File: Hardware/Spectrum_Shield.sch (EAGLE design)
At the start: 27 parts, among them IC1 MSGEQ7SOIC, IC2 MSGEQ7SOIC, U1 ARDUINO_R3_SHIELD

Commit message: Fixed Ground Issue
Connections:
- net GND: now also AUDIOJACK1.SLEEVE
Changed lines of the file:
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@@
 <?xml version="1.0" encoding="utf-8"?>
 <!DOCTYPE eagle SYSTEM "eagle.dtd">
-<eagle version="7.2.0">
+<eagle version="7.1.0">
 <drawing>
 <settings>
@@
 <layer number="254" name="cooling" color="7" fill="1" visible="yes" active="yes"/>
 </layers>
-<schematic xreflabel="%F%N/%S" xrefpart="/%S">
+<schematic xreflabel="%F%N/%S" xrefpart="/%S.%C%R">
 <attributes>
 </attributes>
@@
 </segment>
 <segment>
+<label x="175.26" y="73.66" size="1.27" layer="95" rot="R180" xref="yes"/>
+<pinref part="AUDIOJACK1" gate="G$1" pin="SLEEVE"/>
 <wire x1="180.34" y1="73.66" x2="175.26" y2="73.66" width="0.1524" layer="91"/>
-<label x="175.26" y="73.66" size="1.27" layer="95" rot="R180" xref="yes"/>
-</segment>
-<segment>
+</segment>
+<segment>

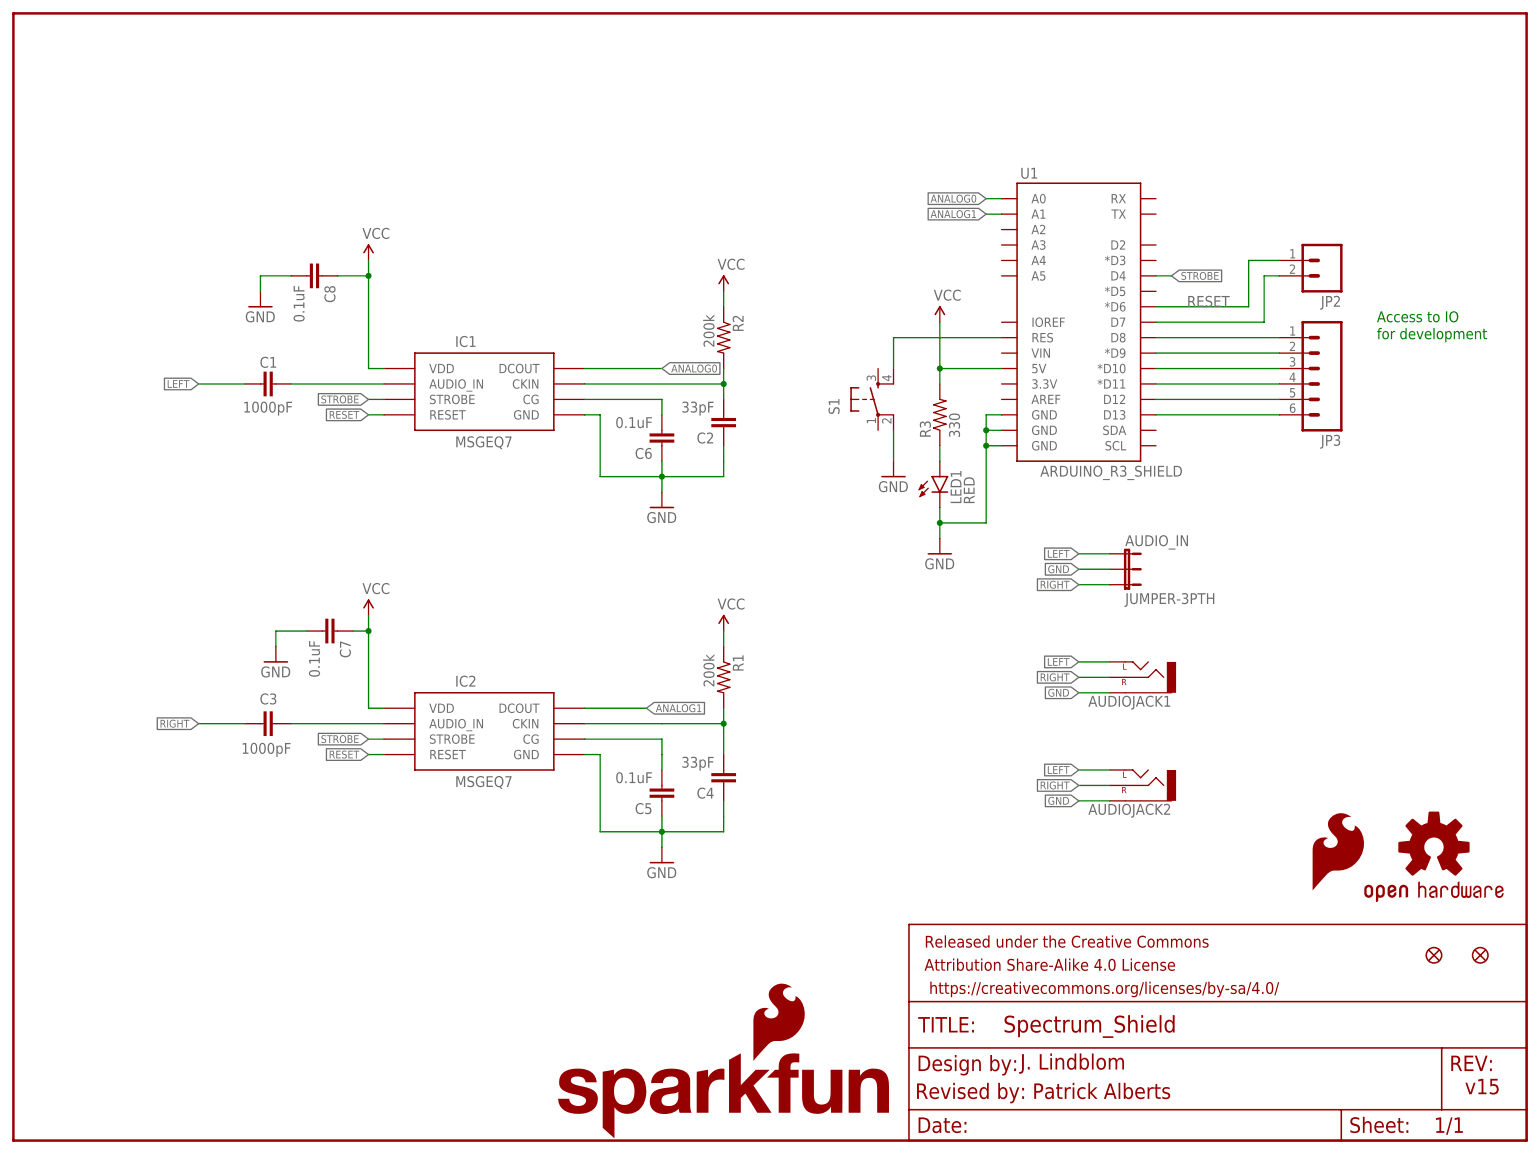
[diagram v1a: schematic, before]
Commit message: QC checklist updated, fixed gnd / pin issue
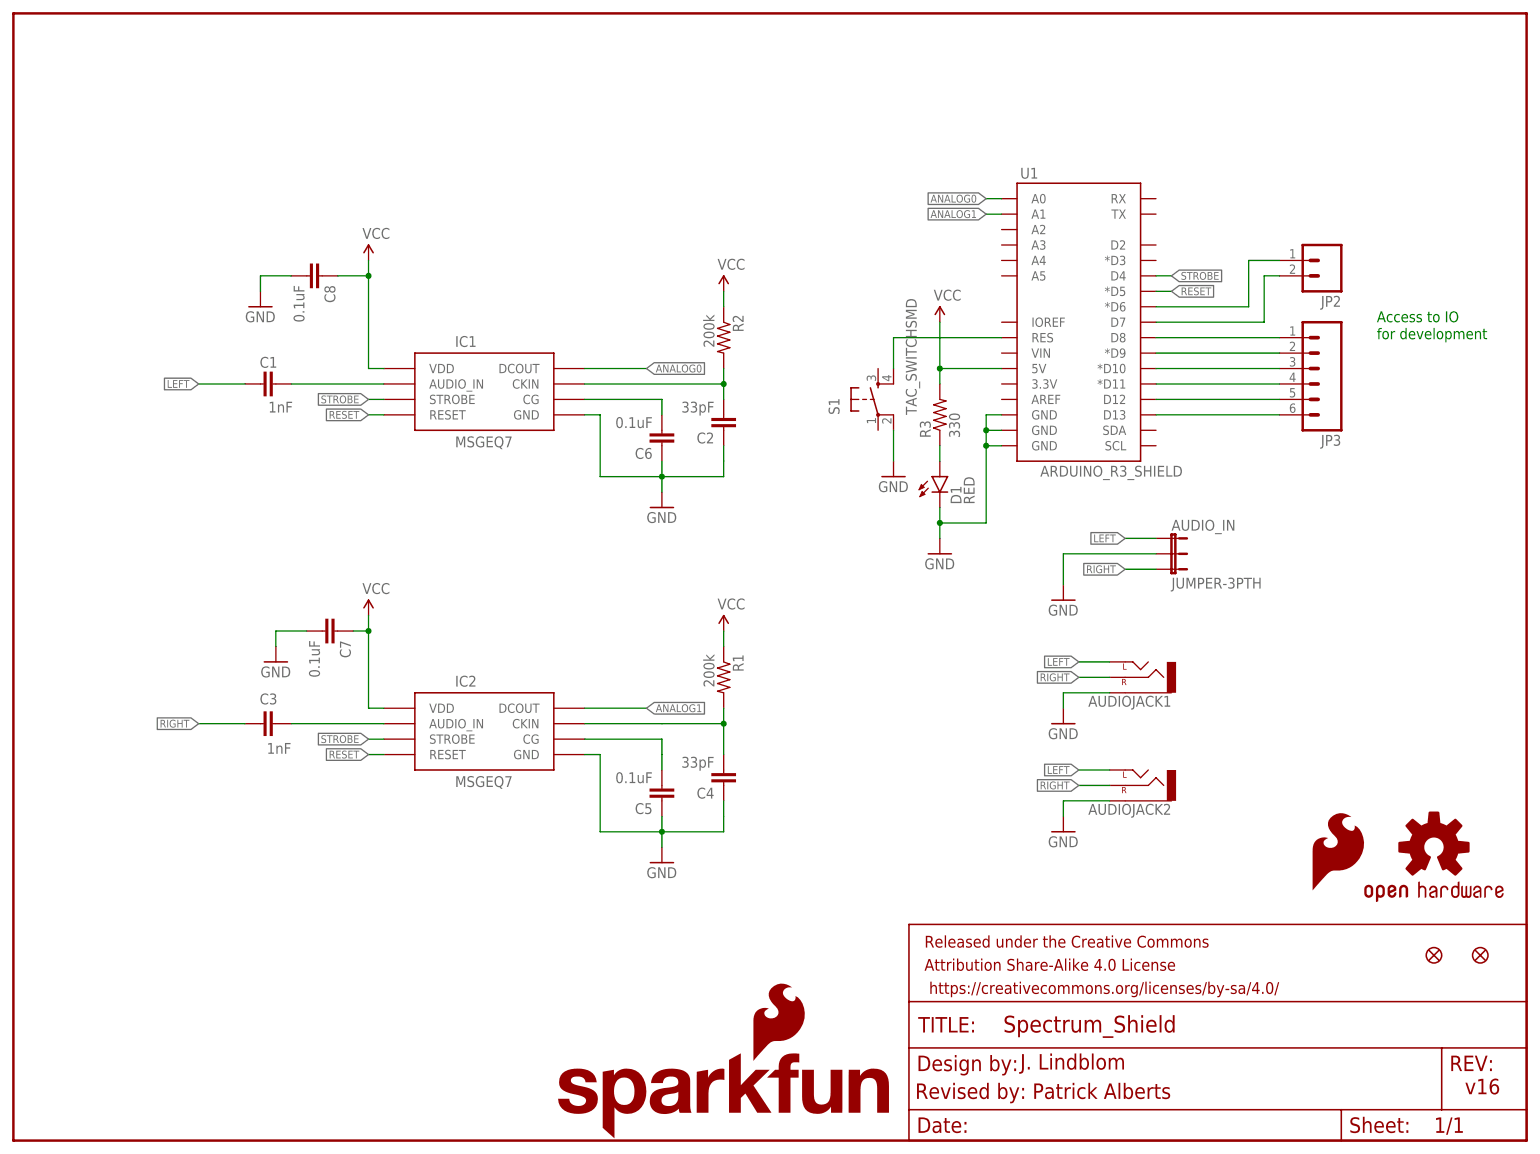
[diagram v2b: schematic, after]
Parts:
- C1, C3: value 1000pF -> 1nF; device SparkFun-Capacitors:CAP0603-CAP -> SparkFun-Capacitors:1NF/1000PF-50V-10%(0603)
- C2, C4: device SparkFun-Capacitors:CAP0603-CAP -> SparkFun-Capacitors:33PF-50V-5%-(0603)
- IC1, IC2: device SparkFun:MSGEQ7SOIC -> SparkFun-AnalogIC:MSGEQ7SOIC
- S1: value (none) -> TAC_SWITCHSMD; device SparkFun:TAC_SWITCHSMD -> SparkFun-Retired:TAC_SWITCHSMD
- renumbered LED1 to D1
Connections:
- new net N$8: JP2.1, U1.*D6
- net RESET: now also U1.*D5; no longer JP2.1, U1.*D6
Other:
- note added: "v16"
- note removed: "v15"
- moved on the sheet: AUDIO_IN

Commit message: Fixed acid traps
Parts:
- removed IC1, IC2: MSGEQ7SOIC, SparkFun-AnalogIC:MSGEQ7SOIC
- added U2, U3: MSGEQ7SOIC, SparkFun-AnalogIC:MSGEQ7SOIC
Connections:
- net ANALOG0: now also U2.DCOUT; no longer IC1.DCOUT
- net ANALOG1: now also U3.DCOUT; no longer IC2.DCOUT
- net GND: now also U2.GND, U3.GND; no longer IC1.GND, IC2.GND
- net N$1: now also U2.AUDIO_IN; no longer IC1.AUDIO_IN
- net N$2: now also U3.AUDIO_IN; no longer IC2.AUDIO_IN
- net N$3: now also U3.CKIN; no longer IC2.CKIN
- net N$4: now also U2.CKIN; no longer IC1.CKIN
- net N$5: now also U3.CG; no longer IC2.CG
- net N$6: now also U2.CG; no longer IC1.CG
- net RESET: now also U2.RESET, U3.RESET; no longer IC1.RESET, IC2.RESET
- net STROBE: now also U2.STROBE, U3.STROBE; no longer IC1.STROBE, IC2.STROBE
- net VCC: now also U2.VDD, U3.VDD; no longer IC1.VDD, IC2.VDD
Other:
- moved on the sheet: AUDIOJACK1, AUDIOJACK2, AUDIO_IN, C1, C2, C3, C4, C5, C6, C7, C8, R1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
